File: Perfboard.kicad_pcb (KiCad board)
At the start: 2 copper layers, 162.6 x 87.6 mm, 1599 parts

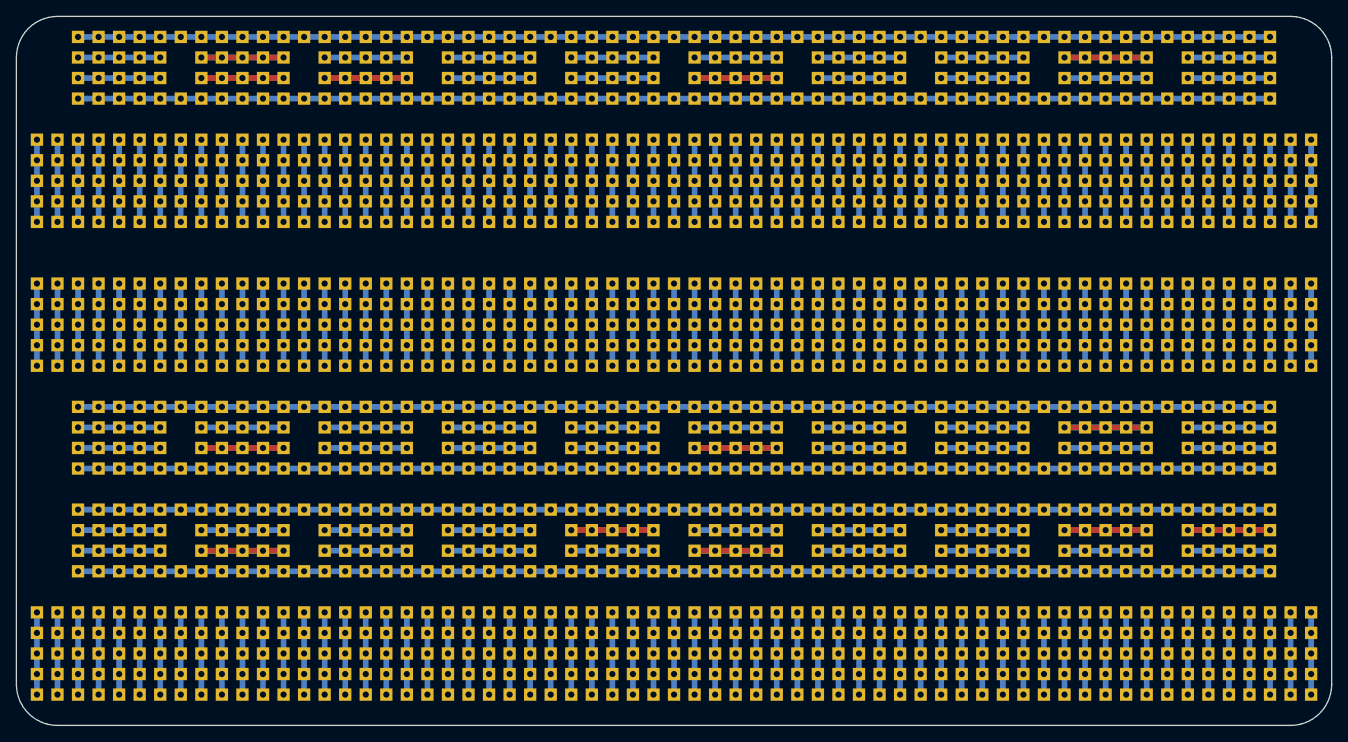
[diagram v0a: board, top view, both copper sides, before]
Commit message: removed traces from the front side
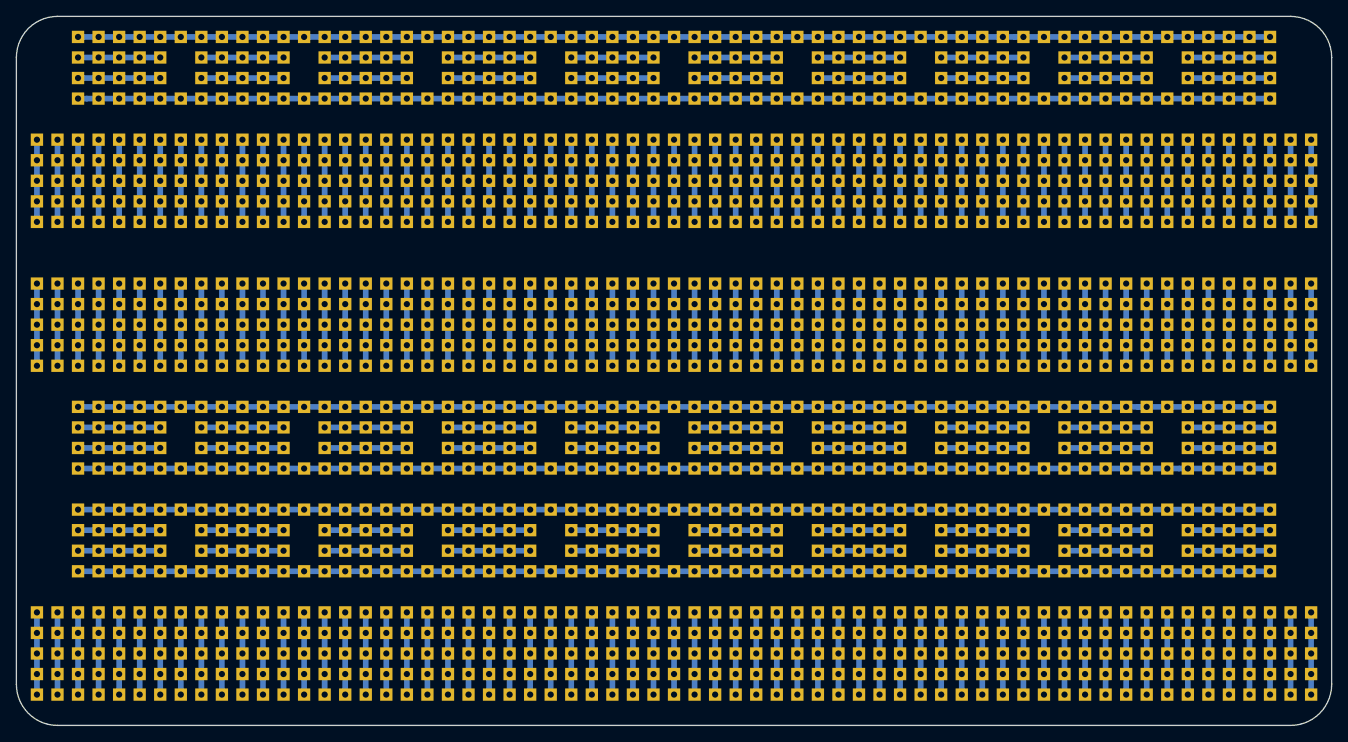
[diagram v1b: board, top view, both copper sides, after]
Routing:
- net (no net): track 3545.8 -> 3413.8 mm
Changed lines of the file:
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@@
-(kicad_pcb (version 20171130) (host pcbnew "(5.1.5)-3")
+(kicad_pcb (version 20171130) (host pcbnew "(5.1.6)-1")
   (general
     (thickness 1.6)
     (drawings 73)
-    (tracks 274)
+    (tracks 261)
     (zones 0)
     (modules 1599)
@@
   (layers
     (0 F.Cu signal)
-    (31 B.Cu signal)
+    (31 B.Cu signal hide)
     (32 B.Adhes user)
     (33 F.Adhes user)
@@
   )
   (setup
-    (last_trace_width 0.7)
+    (last_trace_width 0.25)
     (user_trace_width 0.7)
     (trace_clearance 0.2)
@@
   (segment (start 104.14 27.94) (end 114.3 27.94) (width 0.7) (layer B.Cu) (net 0))
   (segment (start 149.86 25.4) (end 160.02 25.4) (width 0.7) (layer B.Cu) (net 0))
-  (segment (start 43.18 25.4) (end 53.34 25.4) (width 0.7) (layer F.Cu) (net 0))
-  (segment (start 43.18 27.94) (end 53.34 27.94) (width 0.7) (layer F.Cu) (net 0))
-  (segment (start 58.42 27.94) (end 68.58 27.94) (width 0.7) (layer F.Cu) (net 0))
-  (segment (start 104.14 27.94) (end 114.3 27.94) (width 0.7) (layer F.Cu) (net 0))
-  (segment (start 149.86 25.4) (end 160.02 25.4) (width 0.7) (layer F.Cu) (net 0))
-  (segment (start 149.86 83.82) (end 160.02 83.82) (width 0.7) (layer F.Cu) (net 0))
-  (segment (start 104.14 86.36) (end 114.3 86.36) (width 0.7) (layer F.Cu) (net 0))
   (segment (start 43.18 86.36) (end 53.34 86.36) (width 0.7) (layer B.Cu) (net 0))
   (segment (start 104.14 86.36) (end 114.3 86.36) (width 0.7) (layer B.Cu) (net 0))
   (segment (start 149.86 83.82) (end 160.02 83.82) (width 0.7) (layer B.Cu) (net 0))
-  (segment (start 43.18 86.36) (end 53.34 86.36) (width 0.7) (layer F.Cu) (net 0))
-  (segment (start 88.9 83.82) (end 99.06 83.82) (width 0.7) (layer F.Cu) (net 0))
-  (segment (start 165.1 83.82) (end 175.26 83.82) (width 0.7) (layer F.Cu) (net 0))
   (segment (start 43.18 73.66) (end 53.34 73.66) (width 0.7) (layer B.Cu) (net 0))
   (segment (start 104.14 73.66) (end 114.3 73.66) (width 0.7) (layer B.Cu) (net 0))
   (segment (start 149.86 71.12) (end 160.02 71.12) (width 0.7) (layer B.Cu) (net 0))
-  (segment (start 43.18 73.66) (end 53.34 73.66) (width 0.7) (layer F.Cu) (net 0))
-  (segment (start 149.86 71.12) (end 160.02 71.12) (width 0.7) (layer F.Cu) (net 0))
-  (segment (start 104.14 73.66) (end 114.3 73.66) (width 0.7) (layer F.Cu) (net 0))
   (segment (start 22.86 93.98) (end 22.86 104.14) (width 0.7) (layer B.Cu) (net 0))
   (segment (start 25.4 93.98) (end 25.4 104.14) (width 0.7) (layer B.Cu) (net 0))
